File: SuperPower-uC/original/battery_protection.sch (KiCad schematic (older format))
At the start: 11 parts, among them J1 JST_PH_S2B_thru, Q1 DMN2019UTS, U1 AP9101CK6-AYTRG1

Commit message: Update 18650 Battery Holder 3D Model
+ Board 3D Model + 3D box
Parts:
- BT1: footprint Battery:BatteryHolder_Keystone_1042_1x18650 -> BATTERY_CELL_HOLDER_18650_SMT_1042:BatteryHolder_Keystone_1042_1x18650
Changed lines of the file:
@@
 F 0 "BT1" H 3918 1841 50  0000 L CNN
 F 1 "Battery_Cell_Holder_18650_SMT_1042" H 3900 1700 50  0001 L CNN
-F 2 "Battery:BatteryHolder_Keystone_1042_1x18650" V 3800 1760 50  0001 C CNN
+F 2 "BATTERY_CELL_HOLDER_18650_SMT_1042:BatteryHolder_Keystone_1042_1x18650" V 3800 1760 50  0001 C CNN
 F 3 "https://www.keyelco.com/product-pdf.cfm?p=918" V 3800 1760 50  0001 C CNN
 F 4 "Keystone" H 3918 1750 50  0000 L CNN "Mfr_name"

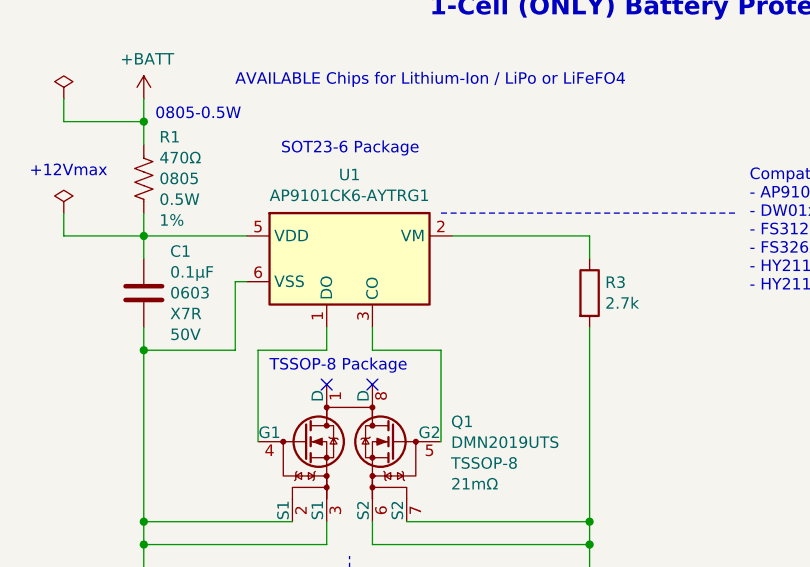
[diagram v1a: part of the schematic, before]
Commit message: Update Placement USB_UART_Bridge
+ Misc.
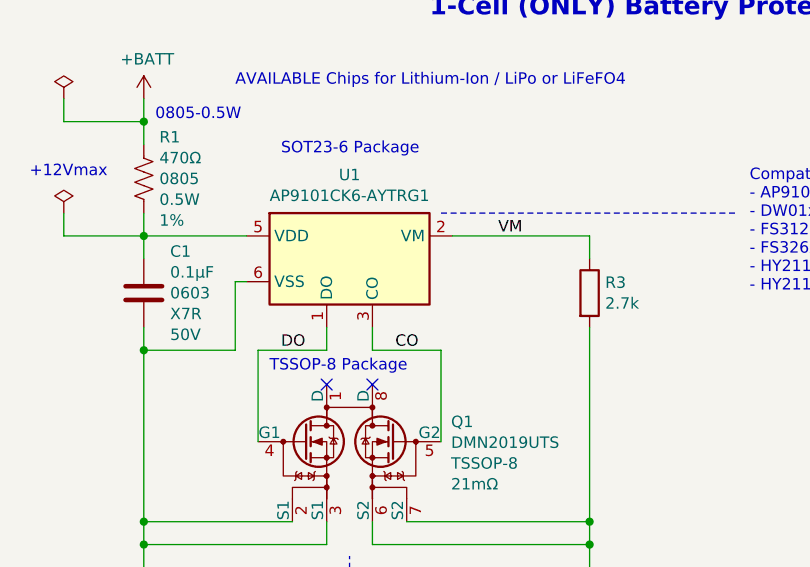
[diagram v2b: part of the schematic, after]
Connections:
- net VM: now reaches R3.1, U1.2 (VM)
- net DO: now reaches Q1.4 (G1), U1.1 (DO)
- net CO: now reaches Q1.5 (G2), U1.3 (CO)
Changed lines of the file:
@@
 	-1   0    0    -1
 $EndComp
+Text Label 3000 4350 0    50   ~ 0
+CO
+Text Label 2500 4350 0    50   ~ 0
+DO
+Text Label 3450 3850 0    50   ~ 0
+VM
 $EndSCHEMATC
